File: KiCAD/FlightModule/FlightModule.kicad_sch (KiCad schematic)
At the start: 24 parts, among them Q1 AO3400A, Q2 AO3400A, U1 ARDUINO_MKR_WAN_1310, U2 MCP2515-xST, U3 MCP2562-E-SN, U4 MB85RQ8MX, U5 MB85RQ8MX, U6 MB85RQ8MX, U7 74AHC1G14, U8 L7805

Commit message: これ階層シートにしないとダメだな
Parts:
- added C3: ~, MKRGPSShield_V4.0:0402-1005X55N, symbol MKRGPSShield_V4.0-eagle-import:Arduino-rcl_C-0402
- added D5: ~, MKRGPSShield_V4.0:SOT65P210X110-3N, symbol MKRGPSShield_V4.0-eagle-import:Arduino-diodes_A2K_SOT-323
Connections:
- net GND: now also C3.2
- net at C2.1, U9.5 (OUT): now also D5.2 (A2)
- net at IC1.17 (VCC): now also IC1.2 (VCC_IO), C3.1, D5.3 (K)
- new net +3V3: D5.1 (A1)
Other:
- moved on the sheet: C1, C2, U9

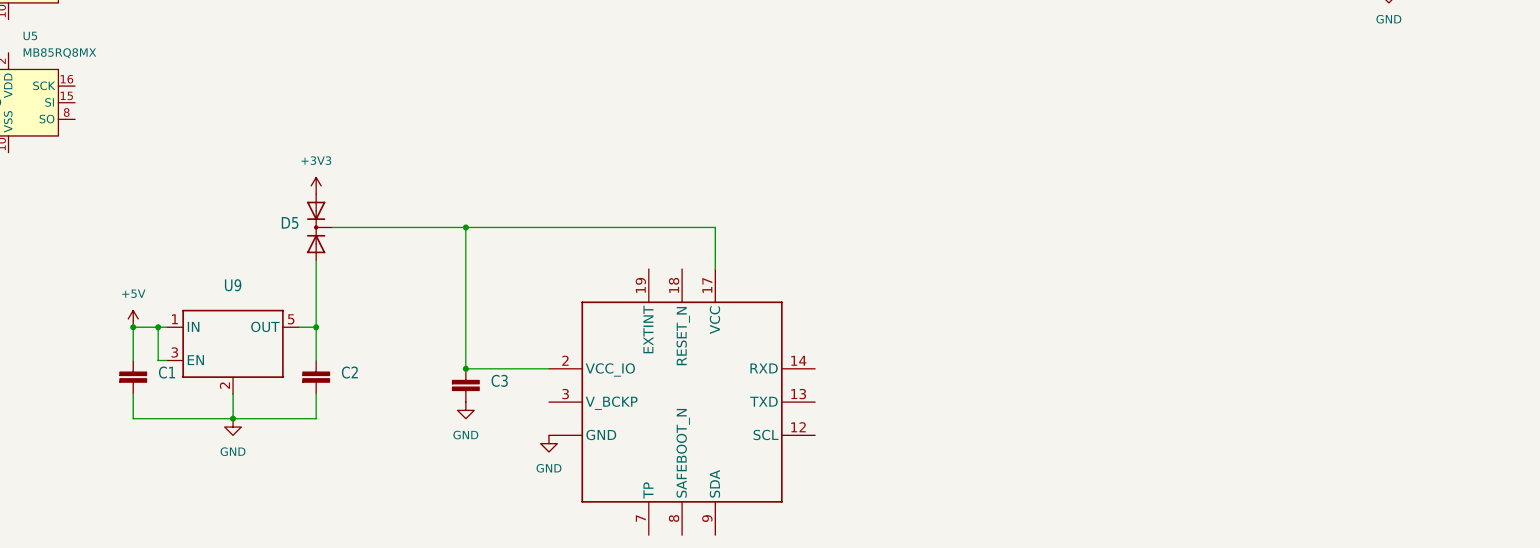
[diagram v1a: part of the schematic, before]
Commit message: 階層シート化した
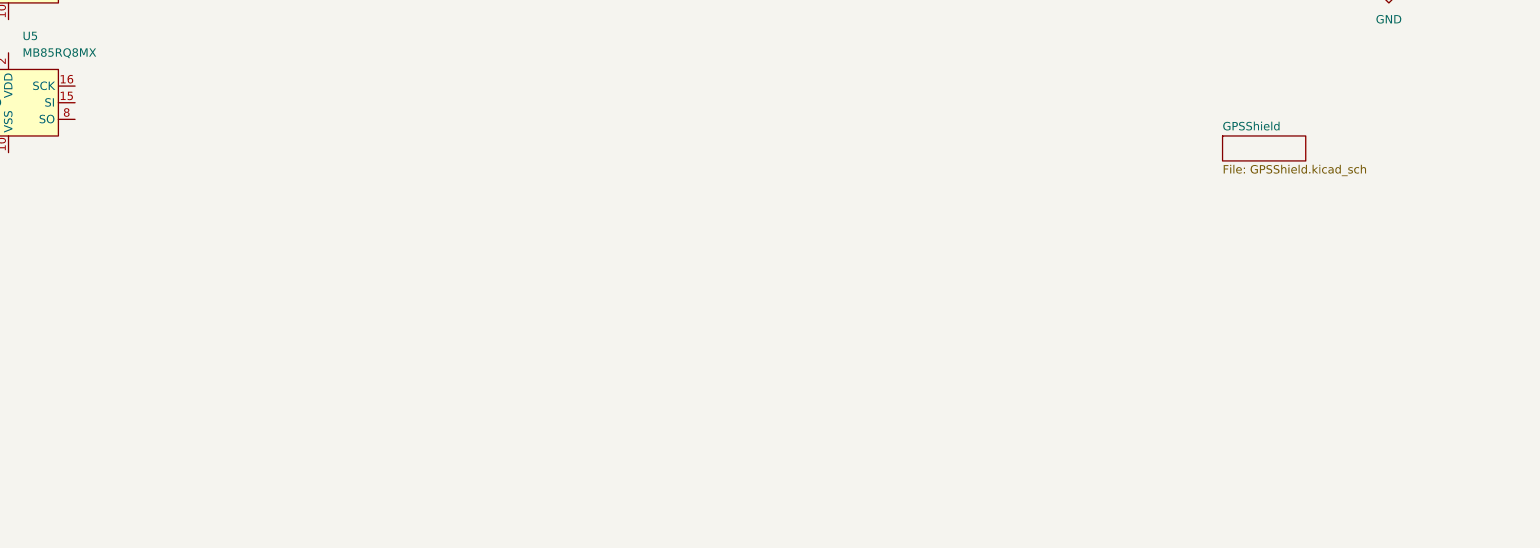
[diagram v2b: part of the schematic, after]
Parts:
- removed C1, C2, C3: ~, MKRGPSShield_V4.0:0402-1005X55N, symbol MKRGPSShield_V4.0-eagle-import:Arduino-rcl_C-0402
- removed D5: ~, MKRGPSShield_V4.0:SOT65P210X110-3N, symbol MKRGPSShield_V4.0-eagle-import:Arduino-diodes_A2K_SOT-323
- removed IC1: ~, GPSShield:UBLOXLIB_SAM-M8Q, symbol MKRGPSShield_V4.0-eagle-import:SAM-M8Q
- removed U9: ~, MKRGPSShield_V4.0:SOT25, symbol MKRGPSShield_V4.0-eagle-import:AP2112K-3.3
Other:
- added sheet GPSShield (GPSShield.kicad_sch)

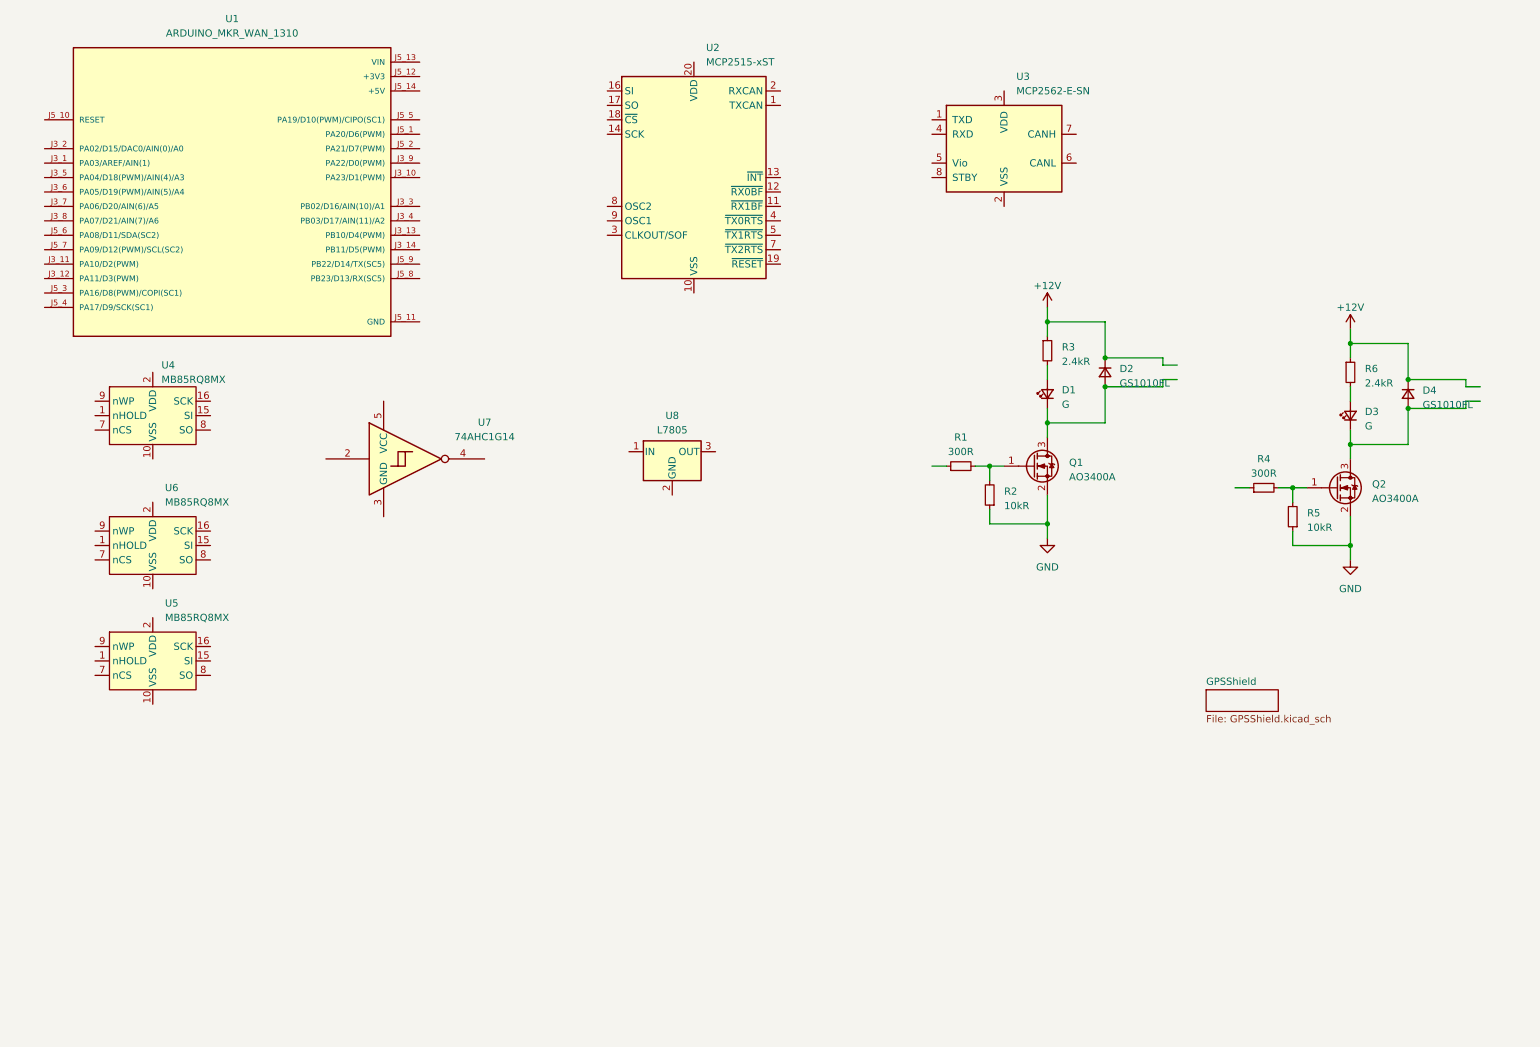
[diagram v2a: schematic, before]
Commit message: MKR周りの配線完了
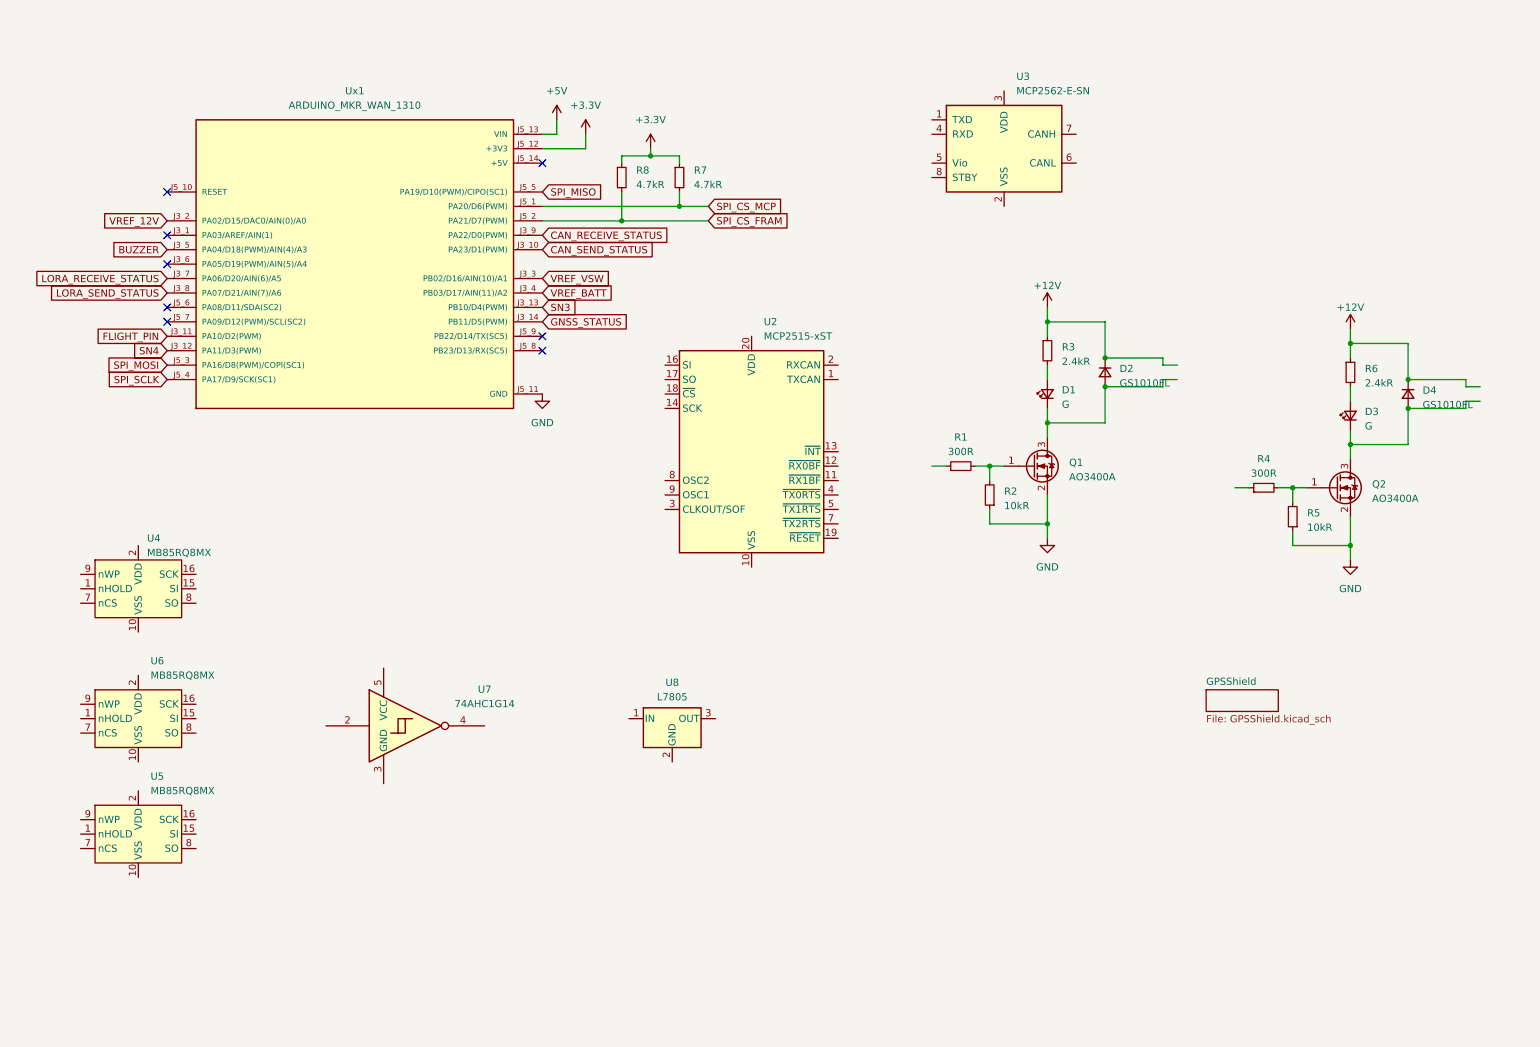
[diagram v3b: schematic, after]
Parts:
- added R7, R8: 4.7kR, symbol Device:R_Small
- renumbered U1 to Ux1
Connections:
- net GND: now also Ux1.J5_11 (GND)
- net CAN_SEND_STATUS: now reaches Ux1.J3_10 (PA23/D1(PWM))
- net FLIGHT_PIN: now reaches Ux1.J3_11 (PA10/D2(PWM))
- net SN4: now reaches Ux1.J3_12 (PA11/D3(PWM))
- net SN3: now reaches Ux1.J3_13 (PB10/D4(PWM))
- net GNSS_STATUS: now reaches Ux1.J3_14 (PB11/D5(PWM))
- net VREF_12V: now reaches Ux1.J3_2 (PA02/D15/DAC0/AIN(0)/A0)
- net VREF_VSW: now reaches Ux1.J3_3 (PB02/D16/AIN(10)/A1)
- net VREF_BATT: now reaches Ux1.J3_4 (PB03/D17/AIN(11)/A2)
- net BUZZER: now reaches Ux1.J3_5 (PA04/D18(PWM)/AIN(4)/A3)
- net LORA_RECEIVE_STATUS: now reaches Ux1.J3_7 (PA06/D20/AIN(6)/A5)
- net LORA_SEND_STATUS: now reaches Ux1.J3_8 (PA07/D21/AIN(7)/A6)
- net CAN_RECEIVE_STATUS: now reaches Ux1.J3_9 (PA22/D0(PWM))
- net SPI_CS_MCP: now reaches Ux1.J5_1 (PA20/D6(PWM))
- net SPI_CS_MCP: now also R7.2
- net +3.3V: now reaches Ux1.J5_12 (+3V3)
- net +3.3V: now also R7.1, R8.1
- net +5V: now reaches Ux1.J5_13 (VIN)
- net SPI_CS_FRAM: now reaches Ux1.J5_2 (PA21/D7(PWM))
- net SPI_CS_FRAM: now also R8.2
- net SPI_MOSI: now reaches Ux1.J5_3 (PA16/D8(PWM)/COPI(SC1))
- net SPI_SCLK: now reaches Ux1.J5_4 (PA17/D9/SCK(SC1))
- net SPI_MISO: now reaches Ux1.J5_5 (PA19/D10(PWM)/CIPO(SC1))
- no-connect marks 0 -> 8
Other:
- moved on the sheet: U2, U4, U5, U6, U7, U8, Ux1

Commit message: メモリ以外完成？
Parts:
- removed D2, D4: GS1010FL, Diode_SMD:D_SOD-123F, symbol Device:D_Small
- removed Q1, Q2: AO3400A, Package_TO_SOT_SMD:SOT-23, symbol Transistor_FET:AO3400A
- removed R6: 2.4kR, Resistor_SMD:R_0603_1608Metric_Pad0.98x0.95mm_HandSolder, symbol Device:R_Small
- removed R7, R8: 4.7kR, symbol Device:R_Small
- removed U2: MCP2515-xST, Package_SO:TSSOP-20_4.4x6.5mm_P0.65mm, symbol Interface_CAN_LIN:MCP2515-xST
- removed U3: MCP2562-E-SN, Package_SO:SOIC-8_3.9x4.9mm_P1.27mm, symbol Interface_CAN_LIN:MCP2562-E-SN
- removed U4: MB85RQ8MX, Package_SO:SOIC-16W_7.5x10.3mm_P1.27mm, symbol Memory_NVRAM:MB85RQ8MX
- removed U5, U6: MB85RQ8MX, Package_SO:SOIC-16W_7.5x10.3mm_P1.27mm, symbol TSRP_IC:MB85RQ8MX
- removed U7: 74AHC1G14, symbol 74xGxx:74AHC1G14
- removed U8: L7805, symbol Regulator_Linear:L7805
- added D2: B, LED_SMD:LED_0603_1608Metric_Pad1.05x0.95mm_HandSolder, symbol Device:LED_Small
- added J1: BUS, Hirose_Connector:Hirose_DF11B-8DP-2DS, symbol Connector_Generic:Conn_01x08
- D1, D3: value G -> B
- R1: value 300R -> 4.7kR
- R2: value 10kR -> 4.7kR
- R3: value 2.4kR -> 680R
- R4: value 300R -> 680R
- R5: value 10kR -> 680R
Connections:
- net +12V: now also J1.1 (Pin_1), J1.2 (Pin_2); no longer R3.1
- net +3.3V: now also R1.1, R2.1
- net GND: now also D1.1 (K), D3.1 (K), D2.1 (K), J1.3 (Pin_3), J1.4 (Pin_4); no longer R2.1, R5.1
- net GNSS_STATUS: now also R5.1
- net LORA_RECEIVE_STATUS: now also R3.1
- net LORA_SEND_STATUS: now also R4.1
- net SPI_CS_FRAM: now also R1.2
- net SPI_CS_MCP: now also R2.2
- net at D3.2 (A): now also R5.2
- net at R4.2: now also D2.2 (A); no longer R5.2
- new net CAN_H: J1.7 (Pin_7), J1.8 (Pin_8)
- new net CAN_L: J1.5 (Pin_5), J1.6 (Pin_6)
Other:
- added sheet CanInterface (CanInterface.kicad_sch)
- added sheet Peripheral (Peripheral.kicad_sch)
- added sheet Power (Power.kicad_sch)
- added sheet Separation (Separation.kicad_sch)

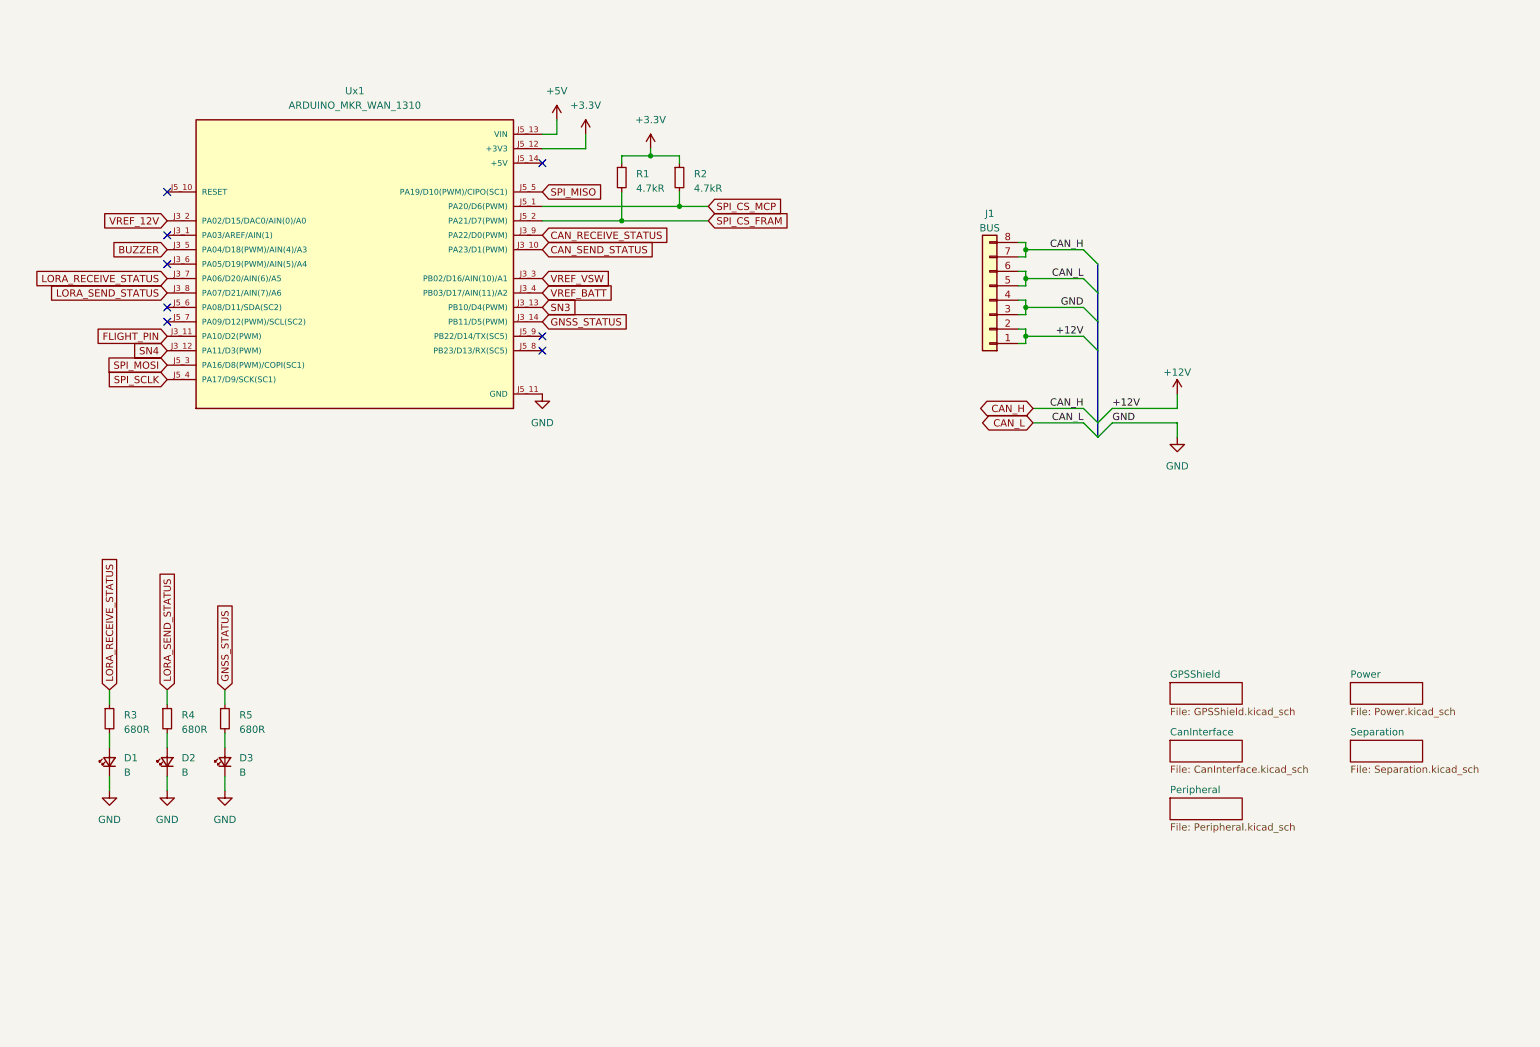
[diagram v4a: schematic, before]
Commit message: CANトランシーバーの配線完了
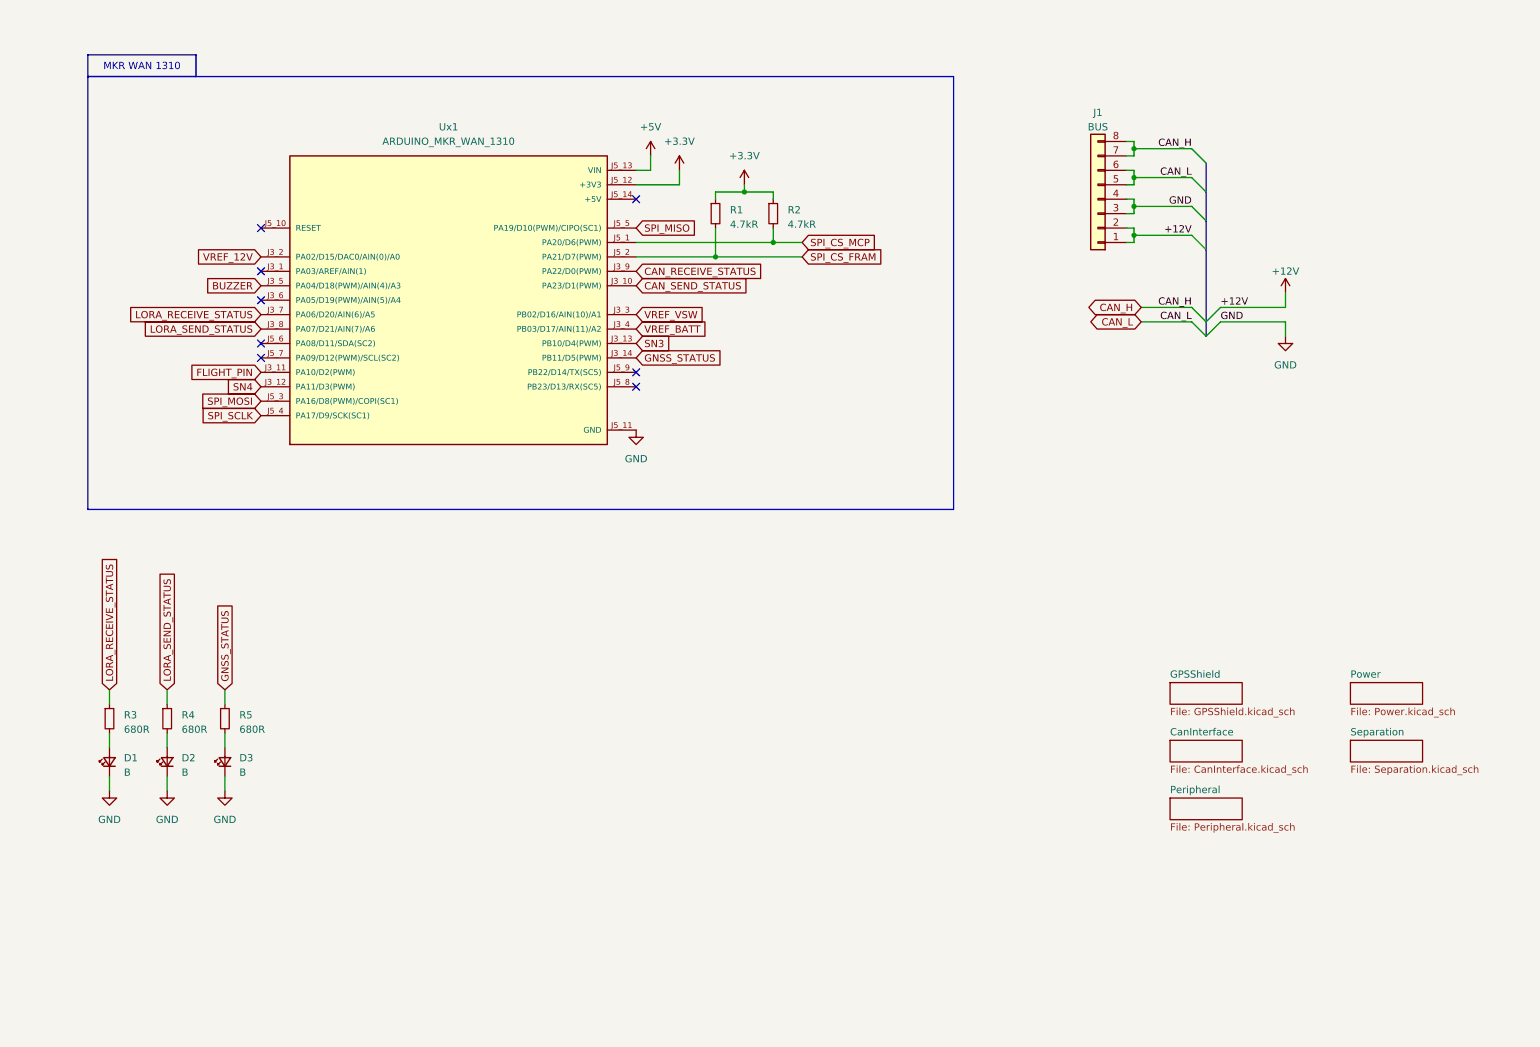
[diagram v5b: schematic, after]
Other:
- moved on the sheet: J1, R1, R2, Ux1

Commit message: バスの回路図完成，LEDの配置を変更
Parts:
- removed J1: BUS, Hirose_Connector:Hirose_DF11B-8DP-2DS, symbol Connector_Generic:Conn_01x08
- added D12, D7: B, LED_SMD:LED_0603_1608Metric_Pad1.05x0.95mm_HandSolder, symbol Device:LED_Small
- added R13, R21: 680R, Resistor_SMD:R_0603_1608Metric_Pad0.98x0.95mm_HandSolder, symbol Device:R_Small
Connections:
- net CAN_RECEIVE_STATUS: now also R13.1
- net CAN_SEND_STATUS: now also R21.1
- net GND: now also D12.1 (K), D7.1 (K)
- new net: D7.2 (A), R13.2
- new net: D12.2 (A), R21.2

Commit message: 回路図8割完成
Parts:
- added R26: 4.7kR, Resistor_SMD:R_0603_1608Metric_Pad0.98x0.95mm_HandSolder, symbol Device:R_Small
- D1, D12, D2, D3, D7: value B -> Blue
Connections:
- net +3.3V: now also R26.1
- net SPI_CS_FRAM renamed SPI_~{CS}_FeRAM0
- net VREF_12V: no longer names the net of Ux1.J3_2 (PA02/D15/DAC0/AIN(0)/A0)
- net VREF_BATT: no longer names the net of Ux1.J3_4 (PB03/D17/AIN(11)/A2)
- net VREF_VSW renamed SPI_~{CS}_FeRAM1
- net SPI_~{CS}_FeRAM1: now also R26.2
- no-connect marks 8 -> 9
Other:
- moved on the sheet: D1, D12, D2, D3, D7, R1, R13, R2, R21, R3, R4, R5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
